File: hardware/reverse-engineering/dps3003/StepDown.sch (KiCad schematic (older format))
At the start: 38 parts, among them J1 IN, J2 OUT, Q0 MMBT3904(1AM), Q1 2N7002, Q2 AOD409, Q6 MMBT2907(2F), U2 6CWQ04, U3 XL7005A, U4 LM321

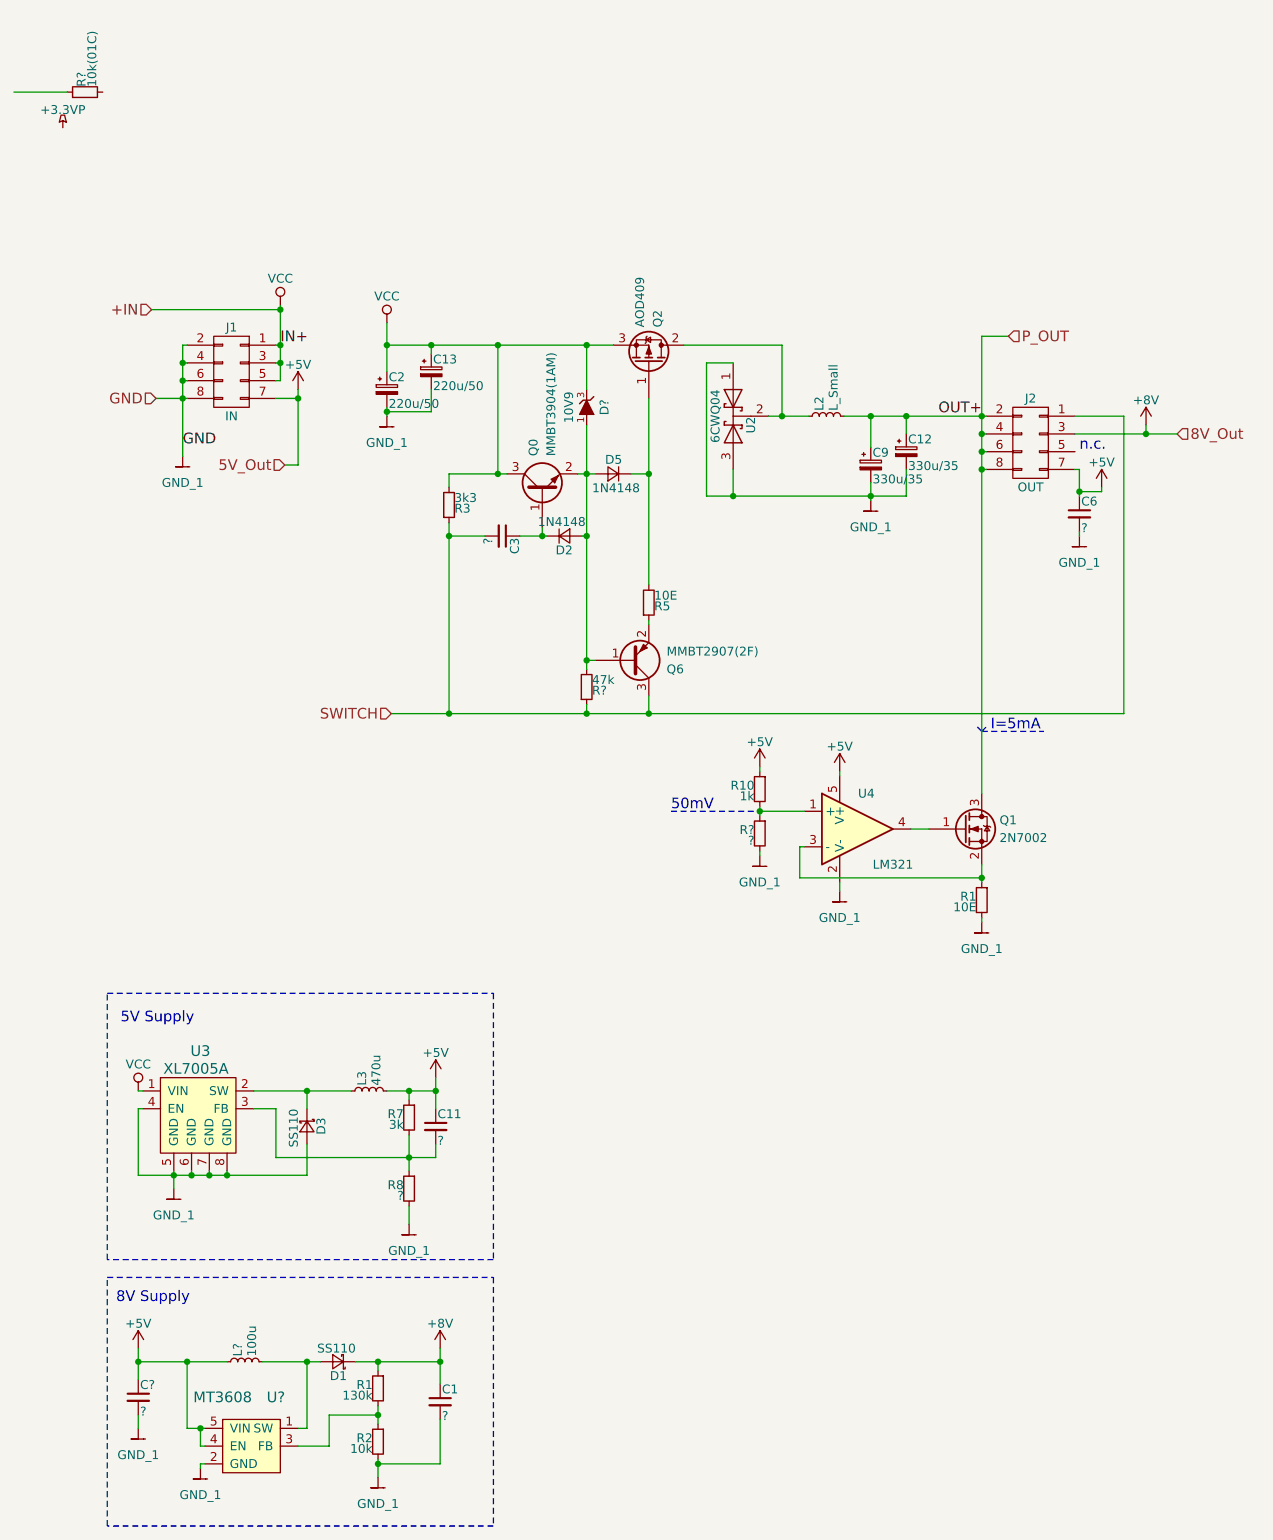
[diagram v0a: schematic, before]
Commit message: Fixed #61
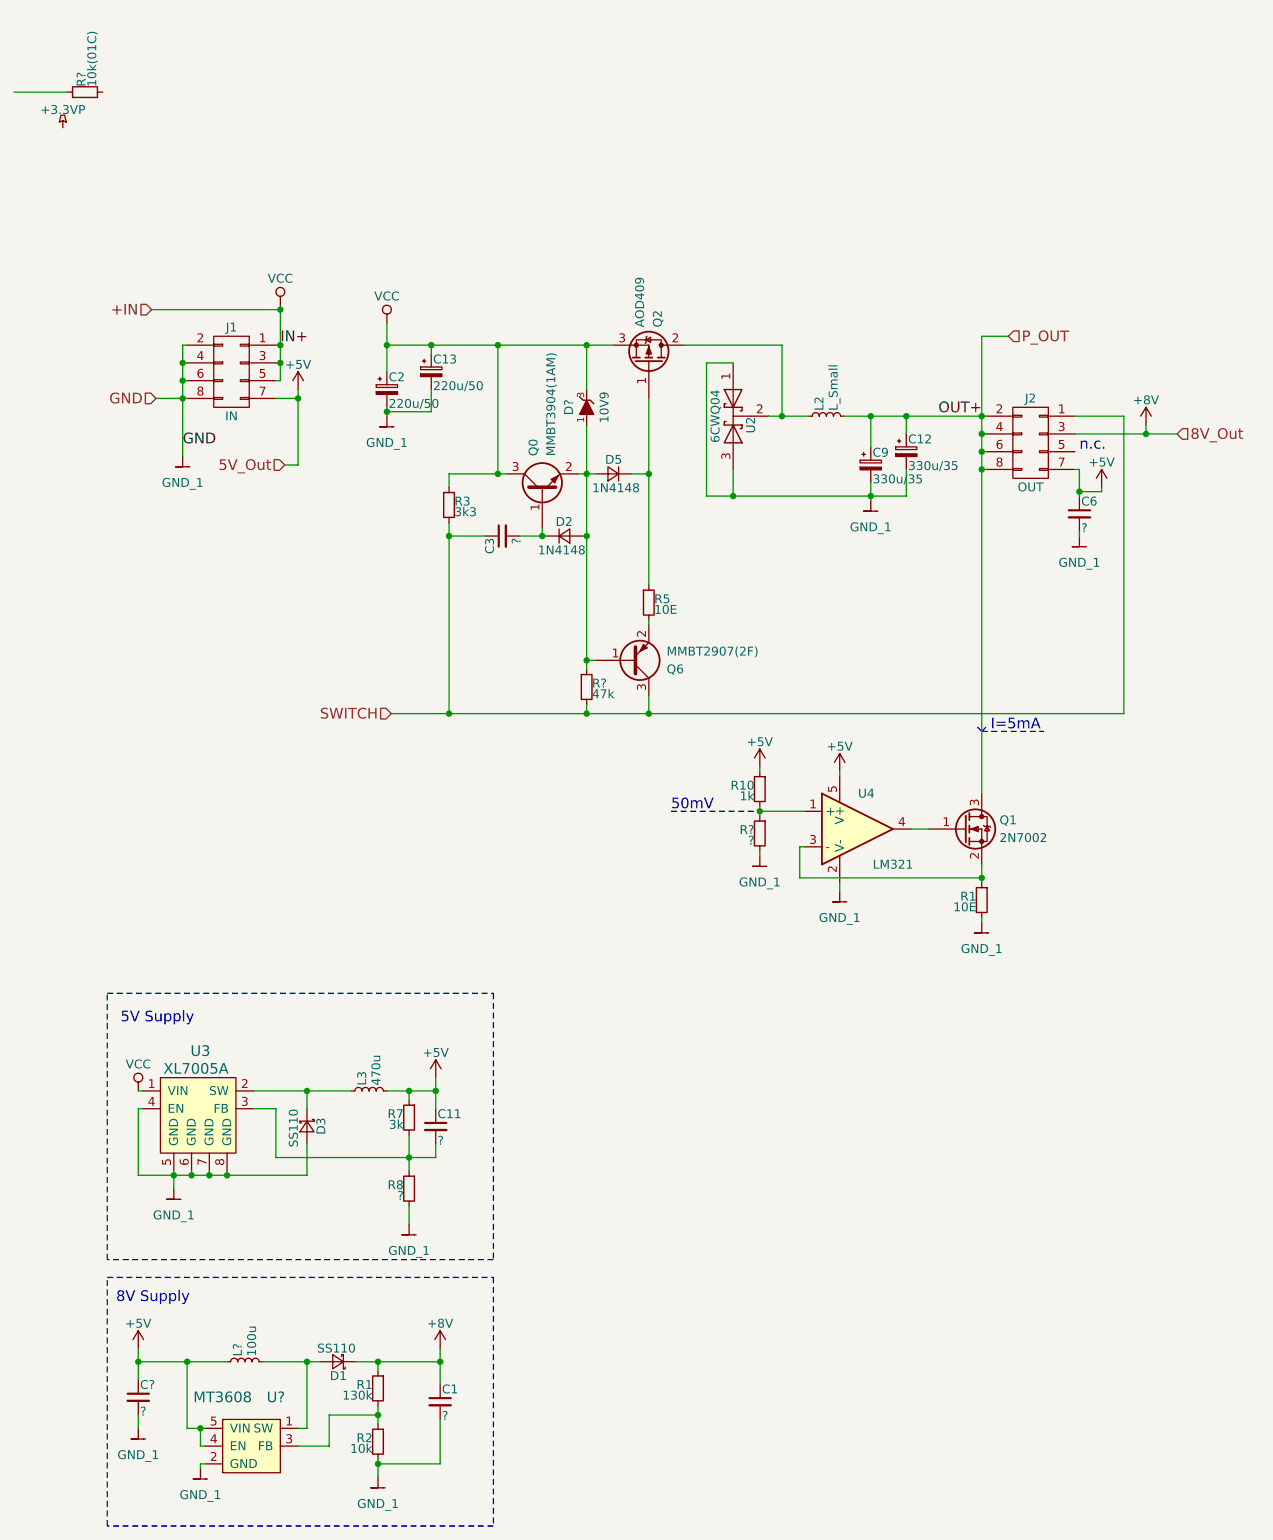
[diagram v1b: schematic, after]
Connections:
- net SWITCH: now also C3.1, R3.2, R?.2; no longer C3.2, R3.1, R?.1
- net VCC: now also R3.1; no longer R3.2
- net at D5.1 (K), Q2.1 (G): now also R5.1; no longer R5.2
- net at D2.1 (K), Q0.1 (B): now also C3.2; no longer C3.1
- net at D2.2 (A), D5.2 (A), D?.1 (A)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: now also R?.1; no longer R?.2
- net at Q6.2 (E): now also R5.2; no longer R5.1
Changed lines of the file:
@@
 LIBS:my_sensors
 LIBS:my_transistors
-LIBS:DPS3203-cache
+LIBS:DPS3003-cache
 EELAYER 25 0
 EELAYER END
@@
 F 3 "" H 3650 2425 50  0001 C CNN
 	1    3650 2425
-	1    0    0    1
+	1    0    0    -1
 $EndComp
 $Comp
@@
 F 3 "" H 3300 2900 50  0001 C CNN
 	1    3300 2900
-	1    0    0    1
+	1    0    0    -1
 $EndComp
 $Comp
@@
 F 3 "" H 3300 1325 50  0000 C CNN
 	1    3300 1325
-	0    1    1    0
+	0    -1   1    0
 $EndComp
 $Comp
@@
 F 3 "" H 2525 1875 50  0001 C CNN
 	1    2525 1875
-	1    0    0    1
+	1    0    0    -1
 $EndComp
 $Comp
@@
 F 3 "" V 3175 2050 50  0001 C CNN
 	1    3175 2050
-	1    0    0    1
+	1    0    0    -1
 $EndComp
 $Comp
@@
 F 3 "" H 2825 2050 50  0001 C CNN
 	1    2825 2050
-	0    1    1    0
+	0    -1   1    0
 $EndComp
 $Comp
@@
 $EndComp
 Wire Wire Line
-	4750 1375 4900 1375
-Wire Wire Line
-	4900 1375 5100 1375
-Wire Wire Line
-	5100 1375 5525 1375
-Wire Wire Line
-	5525 1375 5550 1375
+	4750 1375 5550 1375
 Wire Wire Line
 	5525 1675 5550 1675
@@
 Connection ~ 5525 1375
 Wire Wire Line
-	5525 925  5525 1375
-Wire Wire Line
-	5525 1375 5525 1475
-Wire Wire Line
-	5525 1475 5525 1575
-Wire Wire Line
-	5525 1575 5525 1675
-Wire Wire Line
-	5525 1675 5525 3500
+	5525 925  5525 3500
 Wire Wire Line
 	1575 1175 1550 1175
@@
 	1050 975  1025 975
 Wire Wire Line
-	1025 975  1025 1075
-Wire Wire Line
-	1025 1075 1025 1175
-Wire Wire Line
-	1025 1175 1025 1275
-Wire Wire Line
-	1025 1275 1025 1600
-Wire Wire Line
-	875  1275 1025 1275
-Wire Wire Line
-	1025 1275 1050 1275
+	1025 975  1025 1600
+Wire Wire Line
+	875  1275 1050 1275
 Wire Wire Line
 	1050 1075 1025 1075
@@
 Connection ~ 5100 1375
 Wire Wire Line
-	4900 1750 4900 1825
-Wire Wire Line
-	4900 1825 4900 1850
-Wire Wire Line
-	3975 1825 4125 1825
-Wire Wire Line
-	4125 1825 4900 1825
-Wire Wire Line
-	4900 1825 5100 1825
+	4900 1750 4900 1850
+Wire Wire Line
+	3975 1825 5100 1825
 Wire Wire Line
 	5100 1825 5100 1675
@@
 	4125 1825 4125 1675
 Wire Wire Line
-	4325 1375 4400 1375
-Wire Wire Line
-	4400 1375 4550 1375
+	4325 1375 4550 1375
 Wire Wire Line
 	4125 1075 3975 1075
@@
 Connection ~ 4400 1375
 Wire Wire Line
-	2175 850  2175 975
-Wire Wire Line
-	2175 975  2175 1125
+	2175 850  2175 1125
 Connection ~ 2175 975
 Wire Wire Line
@@
 Connection ~ 2425 975
 Wire Wire Line
-	2175 1325 2175 1350
-Wire Wire Line
-	2175 1350 2175 1375
+	2175 1325 2175 1375
 Wire Wire Line
 	2175 1350 2425 1350
@@
 	1550 1275 1675 1275
 Wire Wire Line
-	1675 1225 1675 1275
-Wire Wire Line
-	1675 1275 1675 1650
-Wire Wire Line
-	6075 1675 6075 1800
-Wire Wire Line
-	6075 1800 6075 1825
+	1675 1225 1675 1650
+Wire Wire Line
+	6075 1675 6075 1825
 Wire Wire Line
 	6075 1675 6050 1675
 Wire Wire Line
-	975  5625 975  5650
-Wire Wire Line
-	975  5650 975  5725
-Wire Wire Line
-	775  5650 975  5650
-Wire Wire Line
-	975  5650 1075 5650
-Wire Wire Line
-	1075 5650 1175 5650
-Wire Wire Line
-	1175 5650 1275 5650
-Wire Wire Line
-	1275 5650 1725 5650
+	975  5625 975  5725
+Wire Wire Line
+	775  5650 1725 5650
 Wire Wire Line
 	1075 5650 1075 5625
@@
 	775  5175 800  5175
 Wire Wire Line
-	1425 5175 1725 5175
-Wire Wire Line
-	1725 5175 1975 5175
+	1425 5175 1975 5175
 Wire Wire Line
 	1725 5275 1725 5175
@@
 Connection ~ 1275 5650
 Wire Wire Line
-	2175 5175 2300 5175
-Wire Wire Line
-	2300 5175 2450 5175
+	2175 5175 2450 5175
 Wire Wire Line
 	2300 5225 2300 5175
@@
 	1550 5275 1550 5550
 Wire Wire Line
-	1550 5550 2300 5550
-Wire Wire Line
-	2300 5550 2450 5550
-Wire Wire Line
-	2300 5425 2300 5550
-Wire Wire Line
-	2300 5550 2300 5625
+	1550 5550 2450 5550
+Wire Wire Line
+	2300 5425 2300 5625
 Wire Wire Line
 	2450 5550 2450 5475
@@
 	5675 925  5525 925
 Wire Wire Line
-	3650 1275 3650 1700
-Wire Wire Line
-	3650 1700 3650 2325
-Wire Wire Line
-	3300 1425 3300 1700
-Wire Wire Line
-	3300 1700 3300 2050
-Wire Wire Line
-	3300 2050 3300 2750
-Wire Wire Line
-	3300 2750 3300 2800
+	3650 1275 3650 2325
+Wire Wire Line
+	3300 1425 3300 2800
 Wire Wire Line
 	3650 2525 3650 2550
 Connection ~ 3300 2750
 Wire Wire Line
-	2200 3050 2525 3050
-Wire Wire Line
-	2525 3050 3300 3050
-Wire Wire Line
-	3300 3050 3650 3050
-Wire Wire Line
-	3650 3050 6325 3050
+	2200 3050 6325 3050
 Wire Wire Line
 	3650 3050 3650 2950
 Connection ~ 3300 3050
 Wire Wire Line
-	3250 1700 3300 1700
-Wire Wire Line
-	3300 1700 3350 1700
+	3250 1700 3350 1700
 Connection ~ 1575 775
 Wire Wire Line
-	1575 750  1575 775
-Wire Wire Line
-	1575 775  1575 975
-Wire Wire Line
-	1575 975  1575 1075
-Wire Wire Line
-	1575 1075 1575 1175
+	1575 750  1575 1175
 Wire Wire Line
 	3300 3000 3300 3050
 Wire Wire Line
-	2525 1975 2525 2050
-Wire Wire Line
-	2525 2050 2525 3050
+	2525 1975 2525 3050
 Connection ~ 2525 3050
 Connection ~ 3300 1700
@@
 $EndComp
 Wire Wire Line
-	1475 6700 1725 6700
-Wire Wire Line
-	1725 6700 1800 6700
+	1475 6700 1800 6700
 $Comp
 L R_Small R1
@@
 	775  7075 775  7000
 Wire Wire Line
-	775  6625 775  6700
-Wire Wire Line
-	775  6700 775  6800
+	775  6625 775  6800
 Connection ~ 775  6700
 $Comp
@@
 $EndComp
 Wire Wire Line
-	2125 7250 2125 7275
-Wire Wire Line
-	2125 7275 2125 7350
+	2125 7250 2125 7350
 Wire Wire Line
 	2125 7275 2475 7275
@@
 	2475 7275 2475 7025
 Wire Wire Line
-	2000 6700 2125 6700
-Wire Wire Line
-	2125 6700 2475 6700
-Wire Wire Line
-	2475 6625 2475 6700
-Wire Wire Line
-	2475 6700 2475 6825
+	2000 6700 2475 6700
+Wire Wire Line
+	2475 6625 2475 6825
 Wire Wire Line
 	2125 6750 2125 6700
 Connection ~ 2125 6700
 Wire Wire Line
-	2125 6950 2125 7000
-Wire Wire Line
-	2125 7000 2125 7050
+	2125 6950 2125 7050
 Connection ~ 2125 7275
 $Comp
@@
 	6075 2025 6075 2050
 Wire Wire Line
-	6050 1475 6450 1475
-Wire Wire Line
-	6450 1475 6625 1475
+	6050 1475 6625 1475
 Connection ~ 2475 6700
 Text HLabel 6625 1475 2    60   Input ~ 0
@@
 	1125 7175 1125 7075
 Wire Wire Line
-	1050 7075 1125 7075
-Wire Wire Line
-	1125 7075 1150 7075
+	1050 7075 1150 7075
 Wire Wire Line
 	1050 7075 1050 6700
@@
 $EndComp
 Wire Wire Line
-	2450 5100 2450 5175
-Wire Wire Line
-	2450 5175 2450 5275
+	2450 5100 2450 5275
 $Comp
 L +5V #PWR?
@@
 $EndComp
 Wire Wire Line
-	775  6700 1050 6700
-Wire Wire Line
-	1050 6700 1275 6700
+	775  6700 1275 6700
 Wire Wire Line
 	1675 1650 1600 1650
@@
 $EndComp
 Wire Wire Line
-	2175 975  2425 975
-Wire Wire Line
-	2425 975  2800 975
-Wire Wire Line
-	2800 975  3300 975
-Wire Wire Line
-	3300 975  3450 975
+	2175 975  3450 975
 Wire Wire Line
 	1550 975  1575 975
 Wire Wire Line
-	2925 2050 3050 2050
-Wire Wire Line
-	3050 2050 3075 2050
+	2925 2050 3075 2050
 Wire Wire Line
 	3050 2050 3050 2000
@@
 	2525 2050 2725 2050
 Wire Wire Line
-	2525 1700 2800 1700
-Wire Wire Line
-	2800 1700 2850 1700
+	2525 1700 2850 1700
 Wire Wire Line
 	2800 1700 2800 975
@@
 $EndComp
 Wire Wire Line
-	4275 3575 4275 3600
-Wire Wire Line
-	4275 3600 4275 3625
+	4275 3575 4275 3625
 Wire Wire Line
 	4275 3825 4275 3850
@@
 	5525 4200 5525 4225
 Wire Wire Line
-	5525 3900 5525 3975
-Wire Wire Line
-	5525 3975 5525 4000
+	5525 3900 5525 4000
 Wire Wire Line
 	4500 3975 5525 3975
